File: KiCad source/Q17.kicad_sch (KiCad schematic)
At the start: 80 parts, among them J1 Input, J2 Screw_Terminal_01x02, J3 Screw_Terminal_01x03, Q1 IRF610, Q10 2SA970, Q11 BS250, Q12 2SC2240 / AC181, Q13 IRF610, Q14 IRF9610, Q15 FQA46N15, Q16 FQA36P15, Q2 2SA970, Q3 2SC2240, Q4 IRF9610, Q5 FQP3P20, Q6 FQP3N30, Q7 2SC2240, Q8 2N7000, Q9 BS250, U1 OPA1641

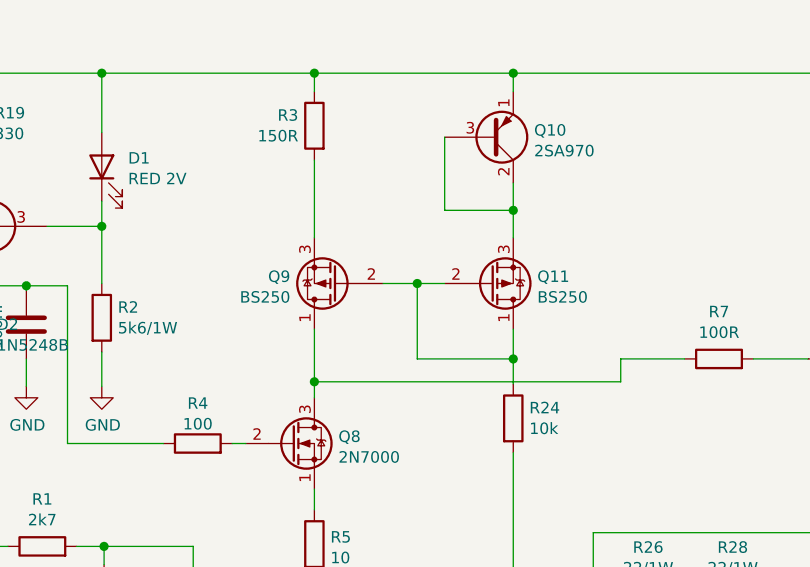
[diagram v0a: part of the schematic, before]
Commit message: BS250 footprint changed for Diodes
There are at least two footprints for BS250 that may be confusing. 
Changes also include:
Smooth traces. 
Reposition of few parts.
Some traces have been enlarged.
Coil was adjusted to take account for other traces with parasitic inductances.
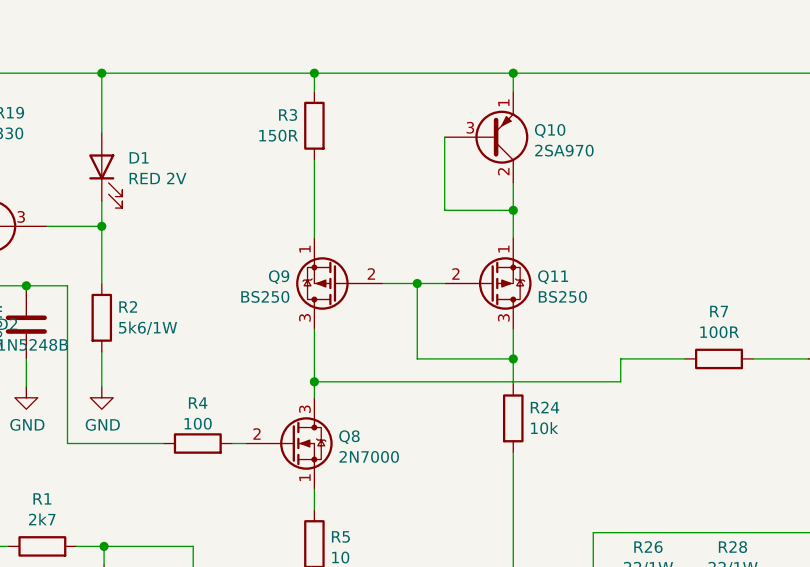
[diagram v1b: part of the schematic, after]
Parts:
- L1: footprint inductor:L -> L:L_new
- Q11, Q9: footprint Package_TO_SOT_THT:TO-92_Inline -> Package_TO_SOT_THT:TO-92L_Inline; symbol Transistor_FET:BS250 -> Transistor_FET:VP0610L
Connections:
- net at Q10.2 (C), Q10.3 (B): now also Q11.1 (S); no longer Q11.3 (S)
- net at Q8.3 (D), R7.1: now also Q9.3 (D); no longer Q9.1 (D)
- net at Q11.2 (G), Q9.2 (G), R24.1: now also Q11.3 (D); no longer Q11.1 (D)
- net at R3.2: now also Q9.1 (S); no longer Q9.3 (S)
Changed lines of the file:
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@@
       (effects (font (size 1.27 1.27)) (justify left))
     )
-    (property "Footprint" "inductor:L" (id 2) (at 177.292 88.9 0)
+    (property "Footprint" "L:L_new" (id 2) (at 177.292 88.9 0)
       (effects (font (size 1.27 1.27)) hide)
     )
@@
     (pin "3")
   )
-  (symbol (lib_id "Transistor_FET:BS250") (at 127.762 48.514 180) (unit 1)
+  (symbol (lib_id "Transistor_FET:VP0610L") (at 127.762 48.514 180) (unit 1)
     (in_bom yes) (on_board yes) (fields_autoplaced)
     (property "Reference" "Q9" (id 0) (at 122.555 47.7531 0)
@@
       (effects (font (size 1.27 1.27)) (justify left))
     )
-    (property "Footprint" "Package_TO_SOT_THT:TO-92_Inline" (id 2) (at 122.682 46.609 0)
+    (property "Footprint" "Package_TO_SOT_THT:TO-92L_Inline" (id 2) (at 122.682 46.609 0)
       (effects (font (size 1.27 1.27) italic) (justify left) hide)
     )
@@
     (pin "3")
   )
-  (symbol (lib_id "Transistor_FET:BS250") (at 144.78 48.514 0) (mirror x) (unit 1)
+  (symbol (lib_id "Transistor_FET:VP0610L") (at 144.78 48.514 0) (mirror x) (unit 1)
     (in_bom yes) (on_board yes) (fields_autoplaced)
     (property "Reference" "Q11" (id 0) (at 149.9871 47.7531 0)
@@
       (effects (font (size 1.27 1.27)) (justify left))
     )
-    (property "Footprint" "Package_TO_SOT_THT:TO-92_Inline" (id 2) (at 149.86 46.609 0)
+    (property "Footprint" "Package_TO_SOT_THT:TO-92L_Inline" (id 2) (at 149.86 46.609 0)
       (effects (font (size 1.27 1.27) italic) (justify left) hide)
     )
@@
     )
     (path "/5db2ed65-75a8-4768-a73d-de03b0ecfc4d"
-      (reference "L1") (unit 1) (value "1u2") (footprint "inductor:L")
+      (reference "L1") (unit 1) (value "1u2") (footprint "L:L_new")
     )
     (path "/cb4618fb-a61b-4f6d-ab22-f977d7e0d481"
@@
     )
     (path "/71158199-e49b-4028-8f47-957a492e31d1"
-      (reference "Q9") (unit 1) (value "BS250") (footprint "Package_TO_SOT_THT:TO-92_Inline")
+      (reference "Q9") (unit 1) (value "BS250") (footprint "Package_TO_SOT_THT:TO-92L_Inline")
     )
     (path "/071ef736-32b9-4357-93dc-ac14efe23e52"
@@
     )
     (path "/9fdbca88-fa8f-4259-aee4-41c049ce2a89"
-      (reference "Q11") (unit 1) (value "BS250") (footprint "Package_TO_SOT_THT:TO-92_Inline")
+      (reference "Q11") (unit 1) (value "BS250") (footprint "Package_TO_SOT_THT:TO-92L_Inline")
     )
     (path "/0176de40-92f3-4877-816b-e22467593d70"

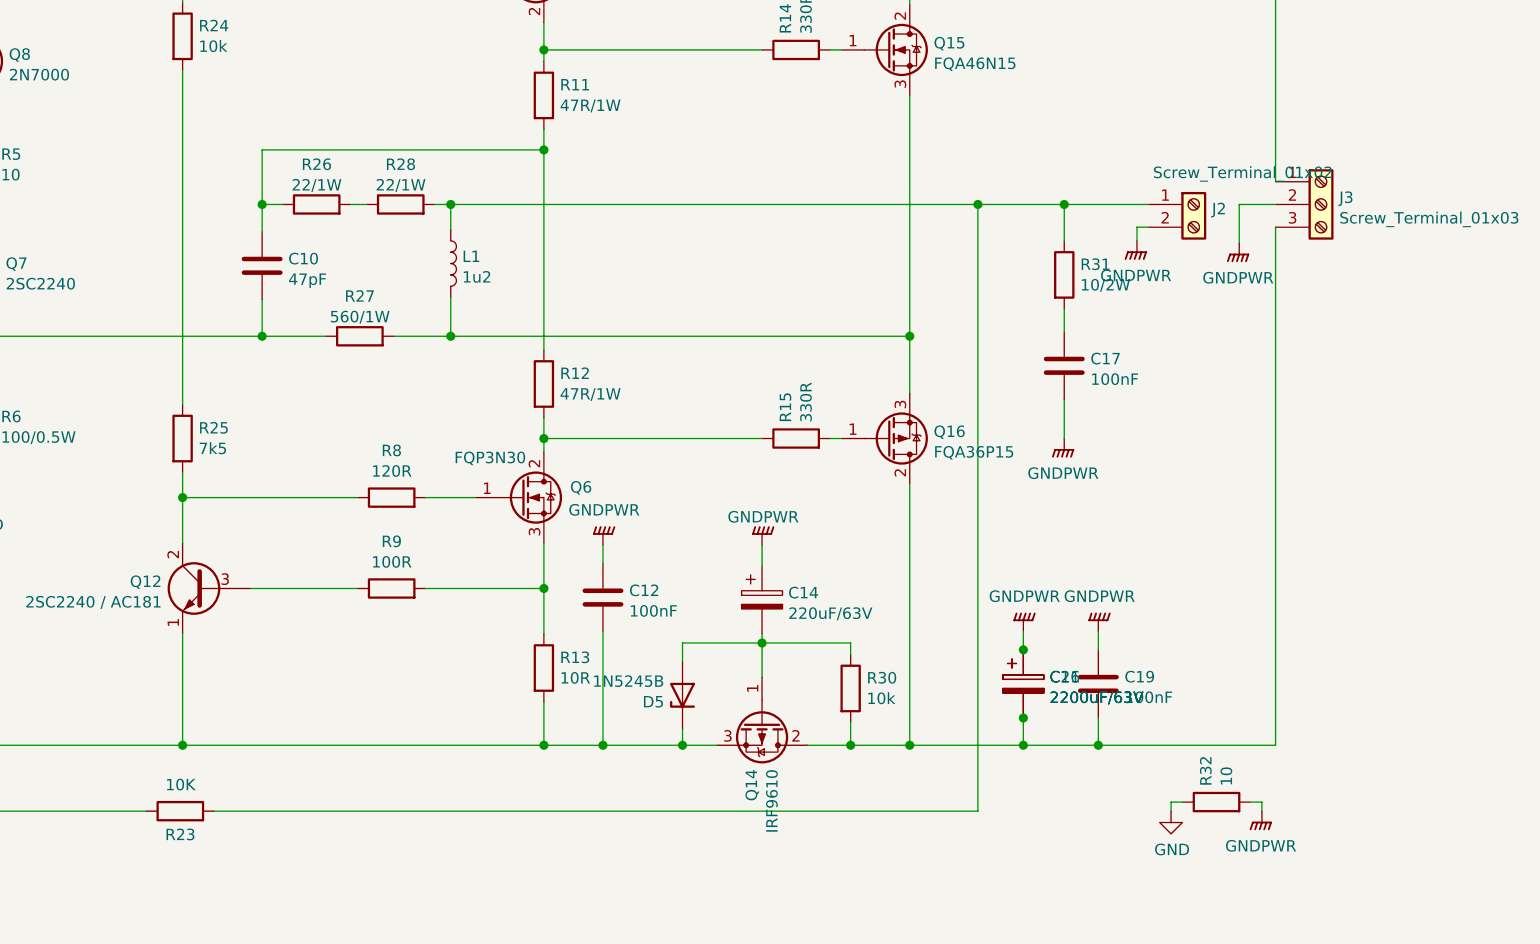
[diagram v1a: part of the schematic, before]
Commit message: Lot of DRC errors have been cleared
There are few DRC errors left due castellated holes and inductor.
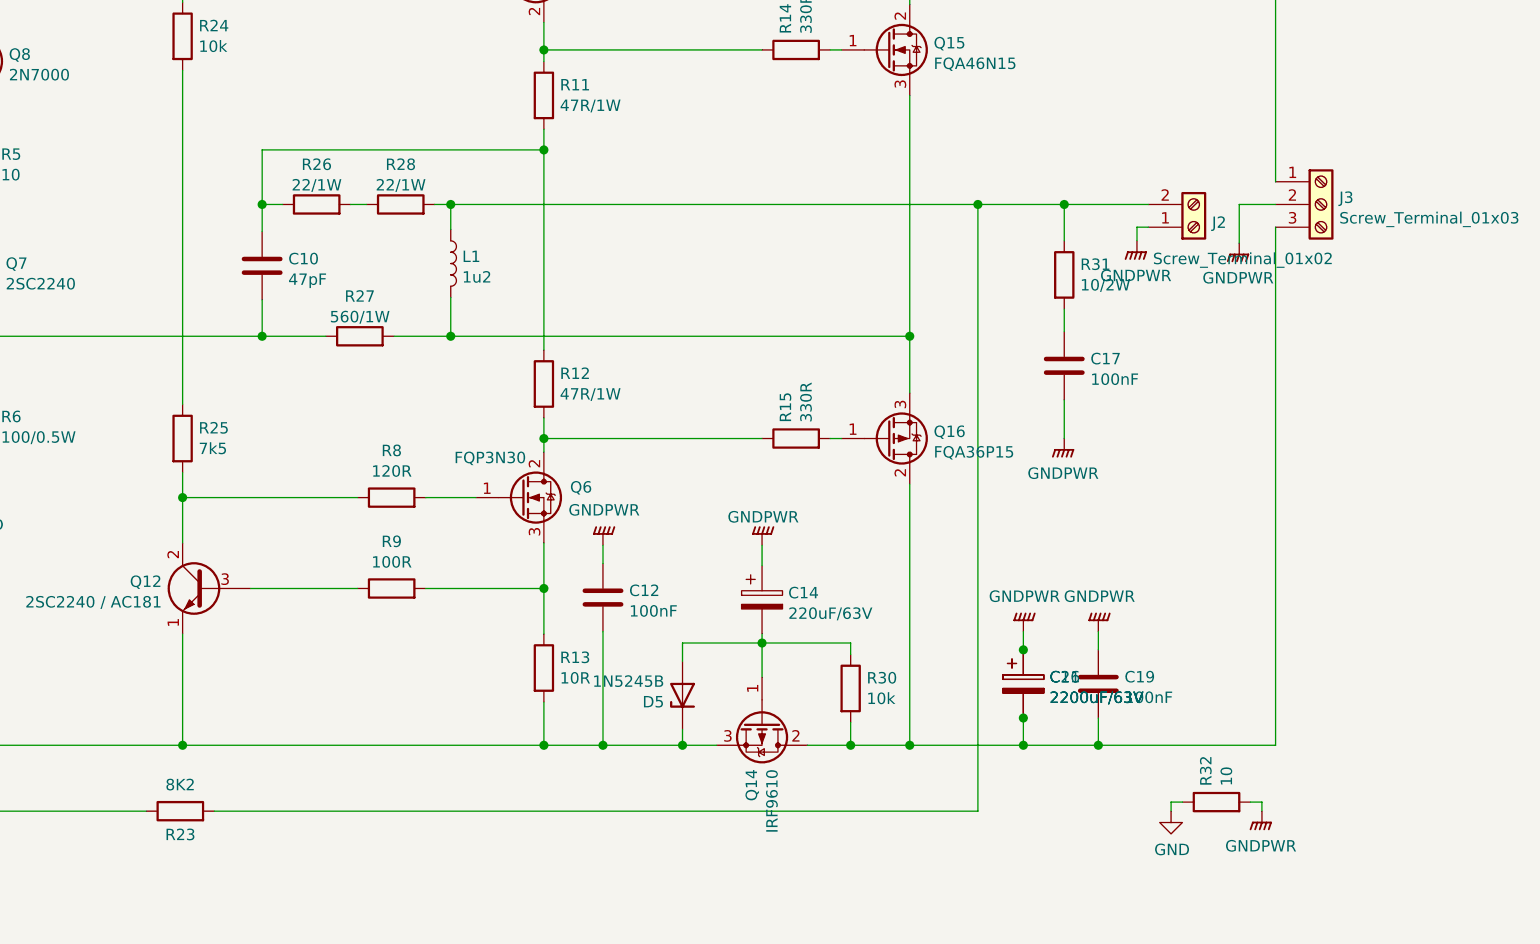
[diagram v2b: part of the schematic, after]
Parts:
- R23: value 10K -> 8K2
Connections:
- net GNDPWR: now also J2.1 (Pin_1); no longer J2.2 (Pin_2)
- net at L1.1, R23.2, R28.2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: now also J2.2 (Pin_2); no longer J2.1 (Pin_1)
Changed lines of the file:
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@@
     (in_bom yes) (on_board yes)
     (property "Reference" "R23" (id 0) (at 147.066 152.7618 90))
-    (property "Value" "10K" (id 1) (at 147.066 147.1865 90))
+    (property "Value" "8K2" (id 1) (at 147.066 147.1865 90))
     (property "Footprint" "Resistor_THT:R_Axial_DIN0207_L6.3mm_D2.5mm_P10.16mm_Horizontal" (id 2) (at 147.066 151.892 90)
       (effects (font (size 1.27 1.27)) hide)
@@
     (pin "2")
   )
-  (symbol (lib_name "Connector:Screw_Terminal_01x02_1") (lib_id "Connector:Screw_Terminal_01x02") (at 260.35 82.296 0) (unit 1)
-    (in_bom yes) (on_board yes)
-    (property "Reference" "J2" (id 0) (at 262.3821 82.8051 0)
-      (effects (font (size 1.27 1.27)) (justify left))
-    )
-    (property "Value" "Screw_Terminal_01x02" (id 1) (at 255.7781 78.7538 0)
-      (effects (font (size 1.27 1.27)) (justify left))
-    )
-    (property "Footprint" "Connector_AMASS:AMASS_XT30U-F_1x02_P5.0mm_Vertical" (id 2) (at 260.35 82.296 0)
-      (effects (font (size 1.27 1.27)) hide)
-    )
-    (property "Datasheet" "~" (id 3) (at 260.35 82.296 0)
+  (symbol (lib_name "Connector:Screw_Terminal_01x02_1") (lib_id "Connector:Screw_Terminal_01x02") (at 260.35 84.836 0) (mirror x) (unit 1)
+    (in_bom yes) (on_board yes)
+    (property "Reference" "J2" (id 0) (at 262.3821 84.3269 0)
+      (effects (font (size 1.27 1.27)) (justify left))
+    )
+    (property "Value" "Screw_Terminal_01x02" (id 1) (at 255.7781 88.3782 0)
+      (effects (font (size 1.27 1.27)) (justify left))
+    )
+    (property "Footprint" "Connector_AMASS:AMASS_XT30U-F_1x02_P5.0mm_Vertical" (id 2) (at 260.35 84.836 0)
+      (effects (font (size 1.27 1.27)) hide)
+    )
+    (property "Datasheet" "~" (id 3) (at 260.35 84.836 0)
       (effects (font (size 1.27 1.27)) hide)
     )
@@
     )
     (path "/ee7cc794-8b46-4e6d-a64c-3ff4ac2fc69d"
-      (reference "R23") (unit 1) (value "10K") (footprint "Resistor_THT:R_Axial_DIN0207_L6.3mm_D2.5mm_P10.16mm_Horizontal")
+      (reference "R23") (unit 1) (value "8K2") (footprint "Resistor_THT:R_Axial_DIN0207_L6.3mm_D2.5mm_P10.16mm_Horizontal")
     )
     (path "/ade798c4-dc18-4049-83f8-3c748354f2fa"
